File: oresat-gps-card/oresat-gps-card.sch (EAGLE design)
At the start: 372 parts, among them J1 ORESAT-DEBUG-CONNECTOR-CARD, J100 DM3BT-DSF-PEJS, J102 FTSH-105-XX-X-DV-K, J4 TFM-120-01-L-D-RA, Q1 MMBT2907, Q2 PMV45EN, Q3 DMP2240UDM, Q4 PMV45EN, Q5 MOSFET-PCH-SOT23-6, Q6 MOSFET-PCH-SOT23-6, U1 RCLAMP0504FB, U10 TLVH431, U11 TCAN330, U12 MIC842LYC5, U13 MIC842LYC5, U14 MAX4211FETE, U15 TPS62112, U16 MAX7310ATE, U17 25AAXX, U18 RCLAMP0504FB, U19 BP2G+, U2 TPS2051CDBVR, U20 MAX8510EXK29+T, U22 LT1719S6, U4 SN74LVC1G07DCK, U5 SKY65723-81, U6 7Q-16.368MBG-T, U7 OSD3358-512M-BSM, U8 MAX8510EXK29+T, U9 MAX8510EXK29+T, Y1 24MHz, Y2 ABS07-32.768KHZ-T

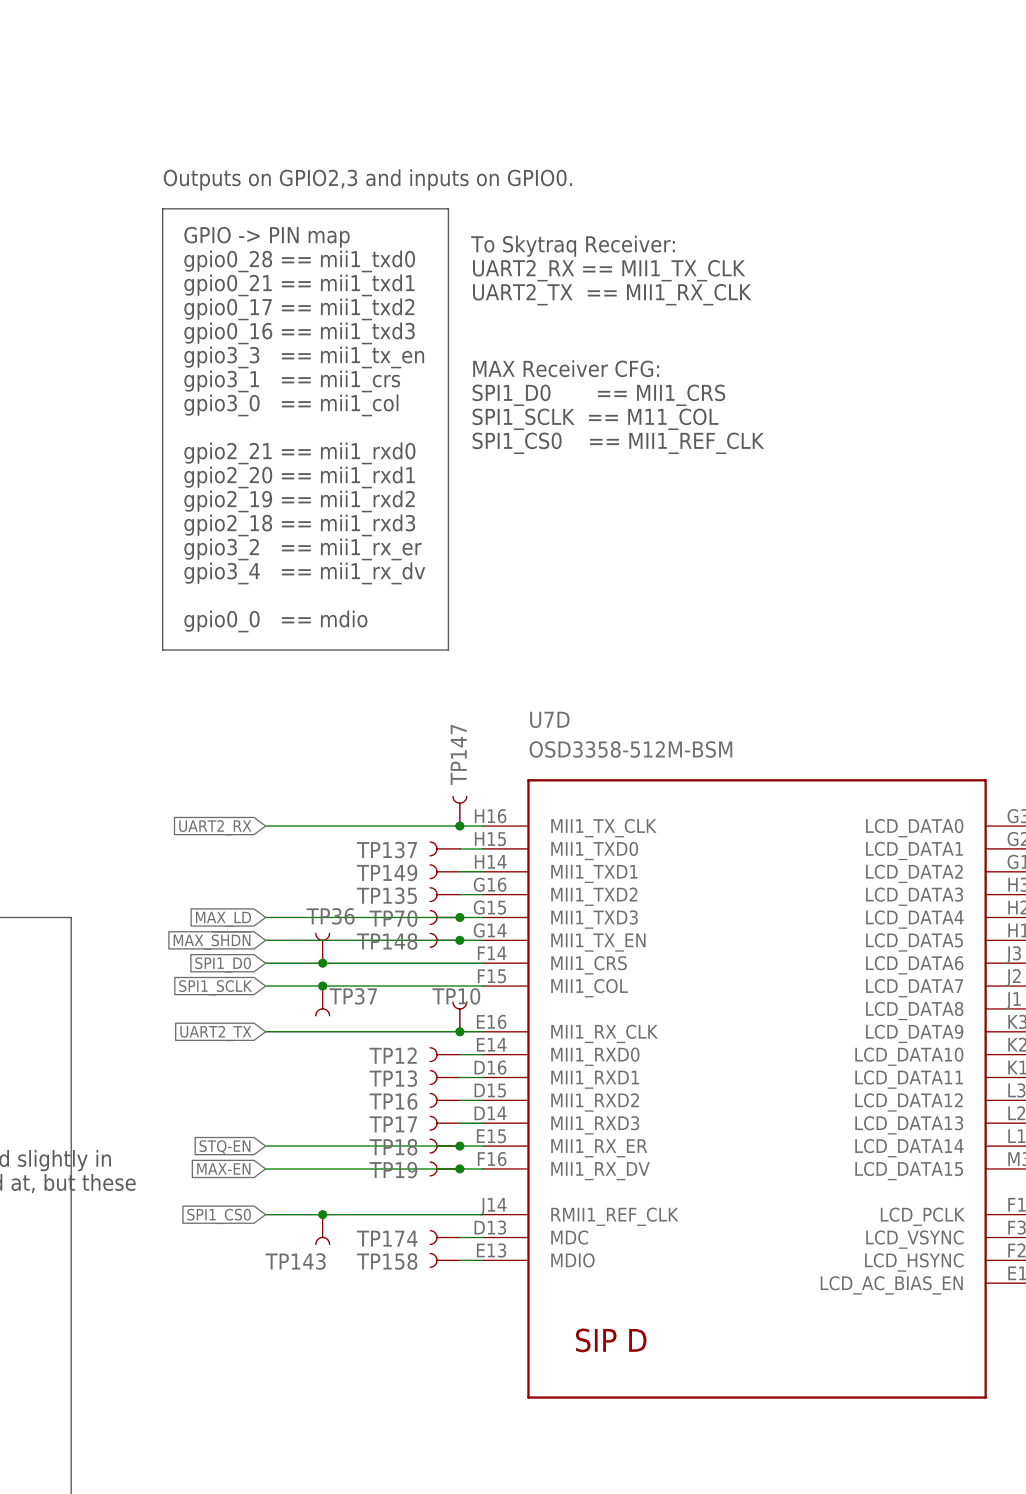
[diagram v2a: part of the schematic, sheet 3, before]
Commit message: Fixed a note in the schematic
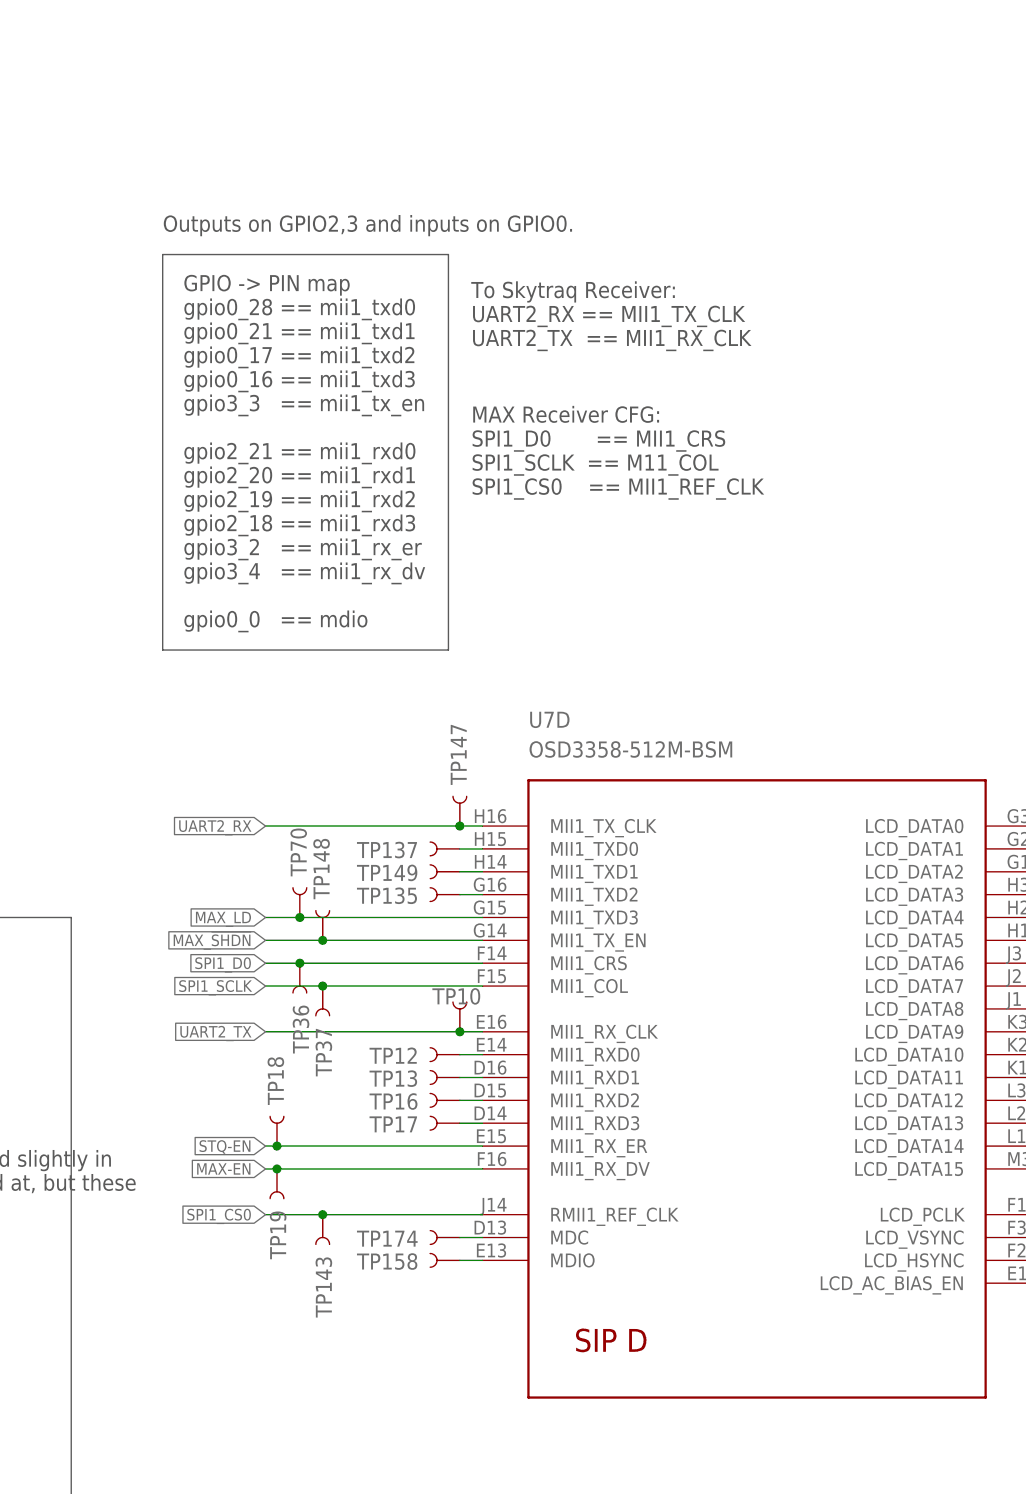
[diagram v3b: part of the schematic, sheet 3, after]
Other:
- note added: "GPIO -> PIN map gpio0_28 == mii1_txd0 gpio0_21 == mii1_txd1 gpio0_17 == mii1_txd2 gpio0_16 == mii1_txd3 gpio3_3 == mii1_tx_en gpio2_21 == mii1_rxd0 gpio2_20 == mii1_rxd1 gpio2_19 == mii1_rxd2 gpio2_18 == mii1_rxd3 gpio3_2 == mii1_rx_er gpio3_4 == mii1_rx_dv gpio0_0 == mdio"
- note removed: "GPIO -> PIN map gpio0_28 == mii1_txd0 gpio0_21 == mii1_txd1 gpio0_17 == mii1_txd2 gpio0_16 == mii1_txd3 gpio3_3 == mii1_tx_en gpio3_1 == mii1_crs gpio3_0 == mii1_col gpio2_21 == mii1_rxd0 gpio2_20 == mii1_rxd1 gpio2_19 == mii1_rxd2 gpio2_18 == mii1_rxd3 gpio3_2 == mii1_rx_er gpio3_4 == mii1_rx_dv gpio0_0 == mdio"
- moved on the sheet: TP148, TP18, TP19, TP36, TP70
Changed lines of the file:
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@@
 gpio0_16 == mii1_txd3
 gpio3_3   == mii1_tx_en
-gpio3_1   == mii1_crs
-gpio3_0   == mii1_col
 gpio2_21 == mii1_rxd0
 gpio2_20 == mii1_rxd1
@@
 gpio3_4   == mii1_rx_dv
 gpio0_0   == mdio </text>
-<text x="538.48" y="459.74" size="1.778" layer="97">Outputs on GPIO2,3 and inputs on GPIO0.</text>
+<text x="538.48" y="454.66" size="1.778" layer="97">Outputs on GPIO2,3 and inputs on GPIO0.</text>
 <wire x1="538.48" y1="408.178" x2="570.23" y2="408.178" width="0.1524" layer="97"/>
-<wire x1="570.23" y1="408.178" x2="570.23" y2="457.2" width="0.1524" layer="97"/>
-<wire x1="570.23" y1="457.2" x2="538.48" y2="457.2" width="0.1524" layer="97"/>
-<wire x1="538.48" y1="457.2" x2="538.48" y2="408.178" width="0.1524" layer="97"/>
+<wire x1="570.23" y1="408.178" x2="570.23" y2="452.12" width="0.1524" layer="97"/>
+<wire x1="570.23" y1="452.12" x2="538.48" y2="452.12" width="0.1524" layer="97"/>
+<wire x1="538.48" y1="452.12" x2="538.48" y2="408.178" width="0.1524" layer="97"/>
 <wire x1="774.7" y1="388.62" x2="774.7" y2="373.38" width="0.1524" layer="97"/>
 <wire x1="774.7" y1="373.38" x2="828.04" y2="373.38" width="0.1524" layer="97"/>
@@
 For SPI boot
 DNP for now</text>
-<text x="572.77" y="447.04" size="1.778" layer="97">To Skytraq Receiver:
+<text x="572.77" y="441.96" size="1.778" layer="97">To Skytraq Receiver:
 UART2_RX == MII1_TX_CLK
 UART2_TX  == MII1_RX_CLK</text>
-<text x="572.77" y="430.53" size="1.778" layer="97">MAX Receiver CFG:
+<text x="572.77" y="425.45" size="1.778" layer="97">MAX Receiver CFG:
 SPI1_D0       == MII1_CRS
 SPI1_SCLK  == M11_COL
@@
 </instance>
 <instance part="TP143" gate="G$1" x="556.26" y="345.44" smashed="yes" rot="R270">
-<attribute name="NAME" x="556.768" y="341.122" size="1.778" layer="95" font="vector" rot="R180"/>
+<attribute name="NAME" x="555.498" y="340.868" size="1.778" layer="95" font="vector" rot="R270"/>
 </instance>
 <instance part="TP174" gate="G$1" x="571.5" y="342.9" smashed="yes" rot="R180">
@@
 <attribute name="NAME" x="357.632" y="298.958" size="1.778" layer="95" font="vector"/>
 </instance>
-<instance part="TP148" gate="G$1" x="571.5" y="375.92" smashed="yes" rot="R180">
-<attribute name="NAME" x="566.928" y="376.682" size="1.778" layer="95" font="vector" rot="R180"/>
+<instance part="TP148" gate="G$1" x="556.26" y="375.92" smashed="yes" rot="R90">
+<attribute name="NAME" x="557.022" y="380.492" size="1.778" layer="95" font="vector" rot="R90"/>
 </instance>
 <instance part="C12" gate="CE" x="464.82" y="332.74" smashed="yes">
@@
 <attribute name="NAME" x="566.928" y="356.362" size="1.778" layer="95" font="vector" rot="R180"/>
 </instance>
-<instance part="TP18" gate="G$1" x="571.5" y="353.06" smashed="yes" rot="R180">
-<attribute name="NAME" x="566.928" y="353.822" size="1.778" layer="95" font="vector" rot="R180"/>
-</instance>
-<instance part="TP19" gate="G$1" x="571.5" y="350.52" smashed="yes" rot="R180">
-<attribute name="NAME" x="566.928" y="351.282" size="1.778" layer="95" font="vector" rot="R180"/>
+<instance part="TP18" gate="G$1" x="551.18" y="353.06" smashed="yes" rot="R90">
+<attribute name="NAME" x="551.942" y="357.632" size="1.778" layer="95" font="vector" rot="R90"/>
+</instance>
+<instance part="TP19" gate="G$1" x="551.18" y="350.52" smashed="yes" rot="R270">
+<attribute name="NAME" x="550.418" y="345.948" size="1.778" layer="95" font="vector" rot="R270"/>
 </instance>
 <instance part="TP20" gate="G$1" x="266.7" y="337.82" smashed="yes" rot="R90">
@@
 <attribute name="NAME" x="263.652" y="324.358" size="1.778" layer="95" font="vector"/>
 </instance>
-<instance part="TP36" gate="G$1" x="556.26" y="373.38" smashed="yes" rot="R90">
-<attribute name="NAME" x="554.482" y="377.698" size="1.778" layer="95" font="vector"/>
+<instance part="TP36" gate="G$1" x="553.72" y="373.38" smashed="yes" rot="R270">
+<attribute name="NAME" x="552.958" y="368.808" size="1.778" layer="95" font="vector" rot="R270"/>
 </instance>
 <instance part="TP37" gate="G$1" x="556.26" y="370.84" smashed="yes" rot="R270">
-<attribute name="NAME" x="557.022" y="368.808" size="1.778" layer="95" font="vector"/>
-</instance>
-<instance part="TP70" gate="G$1" x="571.5" y="378.46" smashed="yes" rot="R180">
-<attribute name="NAME" x="566.928" y="379.222" size="1.778" layer="95" font="vector" rot="R180"/>
+<attribute name="NAME" x="555.498" y="366.268" size="1.778" layer="95" font="vector" rot="R270"/>
+</instance>
+<instance part="TP70" gate="G$1" x="553.72" y="378.46" smashed="yes" rot="R90">
+<attribute name="NAME" x="554.482" y="383.032" size="1.778" layer="95" font="vector" rot="R90"/>
 </instance>
 <instance part="TP71" gate="G$1" x="287.02" y="309.88" smashed="yes" rot="R180">
@@
 <pinref part="TP148" gate="G$1" pin="1"/>
 <pinref part="U7" gate="D" pin="MII1_TX_EN"/>
-<wire x1="571.5" y1="375.92" x2="574.04" y2="375.92" width="0.1524" layer="91"/>
-<wire x1="571.5" y1="375.92" x2="549.91" y2="375.92" width="0.1524" layer="91"/>
-<junction x="571.5" y="375.92"/>
+<wire x1="556.26" y1="375.92" x2="574.04" y2="375.92" width="0.1524" layer="91"/>
+<wire x1="556.26" y1="375.92" x2="549.91" y2="375.92" width="0.1524" layer="91"/>
+<junction x="556.26" y="375.92"/>
 <label x="549.91" y="375.92" size="1.27" layer="95" rot="R180" xref="yes"/>
 </segment>
@@
 <pinref part="U7" gate="D" pin="MII1_RX_ER"/>
 <pinref part="TP18" gate="G$1" pin="1"/>
-<wire x1="571.5" y1="353.06" x2="574.04" y2="353.06" width="0.1524" layer="91"/>
+<wire x1="551.18" y1="353.06" x2="574.04" y2="353.06" width="0.1524" layer="91"/>
 <label x="549.91" y="353.06" size="1.27" layer="95" rot="R180" xref="yes"/>
-<wire x1="571.5" y1="353.06" x2="549.91" y2="353.06" width="0.1524" layer="91"/>
-<junction x="571.5" y="353.06"/>
+<wire x1="551.18" y1="353.06" x2="549.91" y2="353.06" width="0.1524" layer="91"/>
+<junction x="551.18" y="353.06"/>
 </segment>
 </net>
@@
 <pinref part="U7" gate="D" pin="MII1_RX_DV"/>
 <pinref part="TP19" gate="G$1" pin="1"/>
-<wire x1="571.5" y1="350.52" x2="574.04" y2="350.52" width="0.1524" layer="91"/>
+<wire x1="551.18" y1="350.52" x2="574.04" y2="350.52" width="0.1524" layer="91"/>
 <label x="549.91" y="350.52" size="1.27" layer="95" rot="R180" xref="yes"/>
-<wire x1="571.5" y1="350.52" x2="549.91" y2="350.52" width="0.1524" layer="91"/>
-<junction x="571.5" y="350.52"/>
+<wire x1="551.18" y1="350.52" x2="549.91" y2="350.52" width="0.1524" layer="91"/>
+<junction x="551.18" y="350.52"/>
 </segment>
 </net>
@@
 <segment>
 <pinref part="U7" gate="D" pin="MII1_CRS"/>
-<wire x1="574.04" y1="373.38" x2="556.26" y2="373.38" width="0.1524" layer="91"/>
+<wire x1="574.04" y1="373.38" x2="553.72" y2="373.38" width="0.1524" layer="91"/>
 <label x="549.91" y="373.38" size="1.27" layer="95" rot="R180" xref="yes"/>
 <pinref part="TP36" gate="G$1" pin="1"/>
-<wire x1="556.26" y1="373.38" x2="549.91" y2="373.38" width="0.1524" layer="91"/>
-<junction x="556.26" y="373.38"/>
+<wire x1="553.72" y1="373.38" x2="549.91" y2="373.38" width="0.1524" layer="91"/>
+<junction x="553.72" y="373.38"/>
 </segment>
 </net>
@@
 <pinref part="U7" gate="D" pin="MII1_TXD3"/>
 <pinref part="TP70" gate="G$1" pin="1"/>
-<wire x1="571.5" y1="378.46" x2="574.04" y2="378.46" width="0.1524" layer="91"/>
-<wire x1="571.5" y1="378.46" x2="549.91" y2="378.46" width="0.1524" layer="91"/>
-<junction x="571.5" y="378.46"/>
+<wire x1="553.72" y1="378.46" x2="574.04" y2="378.46" width="0.1524" layer="91"/>
+<wire x1="553.72" y1="378.46" x2="549.91" y2="378.46" width="0.1524" layer="91"/>
+<junction x="553.72" y="378.46"/>
 <label x="549.91" y="378.46" size="1.27" layer="95" rot="R180" xref="yes"/>
 </segment>
